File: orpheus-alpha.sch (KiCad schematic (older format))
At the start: 56 parts, among them J1 Signal in, J2 AC in, J3 Signal out, J4 uC, U1 OPA2134, U2 PGA2311, U3 LM317_3PinPackage, U4 LM337_SOT223, U5 LM7805_TO220

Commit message: Small changes, changed output coupling caps to film type
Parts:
- C12, C13: footprint Capacitors_THT:C_Disc_D7.5mm_W4.4mm_P5.00mm -> Capacitors_THT:C_Rect_L7.2mm_W7.2mm_P5.00mm_FKS2_FKP2_MKS2_MKP2
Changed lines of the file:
@@
 F 0 "C12" V 5950 1600 50  0000 C CNN
 F 1 "2.2u" V 5650 1550 50  0000 C CNN
-F 2 "Capacitors_THT:C_Disc_D7.5mm_W4.4mm_P5.00mm" H 5838 1450 50  0001 C CNN
+F 2 "Capacitors_THT:C_Rect_L7.2mm_W7.2mm_P5.00mm_FKS2_FKP2_MKS2_MKP2" H 5838 1450 50  0001 C CNN
 F 3 "" H 5800 1600 50  0001 C CNN
 	1    5800 1600
@@
 F 0 "C13" V 5950 2100 50  0000 C CNN
 F 1 "2.2u" V 5650 2050 50  0000 C CNN
-F 2 "Capacitors_THT:C_Disc_D7.5mm_W4.4mm_P5.00mm" H 5838 1950 50  0001 C CNN
+F 2 "Capacitors_THT:C_Rect_L7.2mm_W7.2mm_P5.00mm_FKS2_FKP2_MKS2_MKP2" H 5838 1950 50  0001 C CNN
 F 3 "" H 5800 2100 50  0001 C CNN
 	1    5800 2100

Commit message: Added part numbers
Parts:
- C1, C2, C3: footprint Capacitors_THT:CP_Radial_D5.0mm_P2.50mm -> Capacitors_THT:CP_Radial_D5.0mm_P2.00mm; Voltage (none) -> 10V; manf# (none) -> UPW1A101MDD
- C10, C11: manf# (none) -> CL10A106MO8NQNC
- C12, C13: manf# (none) -> MKS2C042201K00KSSD
- C14: Voltage (none) -> 25V; manf# (none) -> UBT1E471MPD8
- C15, C16, C8, C9: manf# (none) -> CL10B104JB8NNNC
- C4, C5, C6, C7: Voltage (none) -> 25V; manf# (none) -> UPW1E102MPD6
- Cd1, Cd2, Cd3, Cd4, Cd5: manf# (none) -> 06035C103JAT2A
- D1, D2, D3, D4, D5, D6, D7, D8: manf# (none) -> LL4004G
- D9: Current (none) -> 20mA; manf# (none) -> HSMA-C190
- J1, J3: manf# (none) -> 1715035
- J2: manf# (none) -> 1715022
- J4: manf# (none) -> M20-9970445
- R1, R2, R3, R4: Power (none) -> 1/4 W; Tolerance (none) -> 1%; manf# (none) -> CRCW06031K00FKEAHP
- R10, R7: Power (none) -> 1/4 W; Tolerance (none) -> 1%; manf# (none) -> ERJ-PA3F9100V
- R11: Power (none) -> 1/4 W; Tolerance (none) -> 1%; manf# (none) -> CRCW0603100RFKEAHP
- R12, R13: Power (none) -> 1/4 W; Tolerance (none) -> 1%; manf# (none) -> RCS0603300RFKEA
- R14, R15: Power (none) -> 1/4 W; Tolerance (none) -> 1%; manf# (none) -> CRCW0603100KFKEAHP
- R16: renamed from Rin1; Power (none) -> 1/4 W; Tolerance (none) -> 1%; manf# (none) -> CRCW060356K0FKEAHP
- R17: renamed from Rin2; Power (none) -> 1/4 W; Tolerance (none) -> 1%; manf# (none) -> CRCW060356K0FKEAHP
- R5, R6: Power (none) -> 1 W; Tolerance (none) -> 1%; manf# (none) -> WK73S2JTTE4R70F
- R8, R9: Power (none) -> 1/4 W; Tolerance (none) -> 1%; manf# (none) -> ESR03EZPF2701
- U1: manf# (none) -> OPA2134UA/2K5
- U2: manf# (none) -> PGA2311U
- U3: manf# (none) -> LM317DCYR
- U4: manf# (none) -> LM337IMP/NOPB
- U5: manf# (none) -> LM7805CT

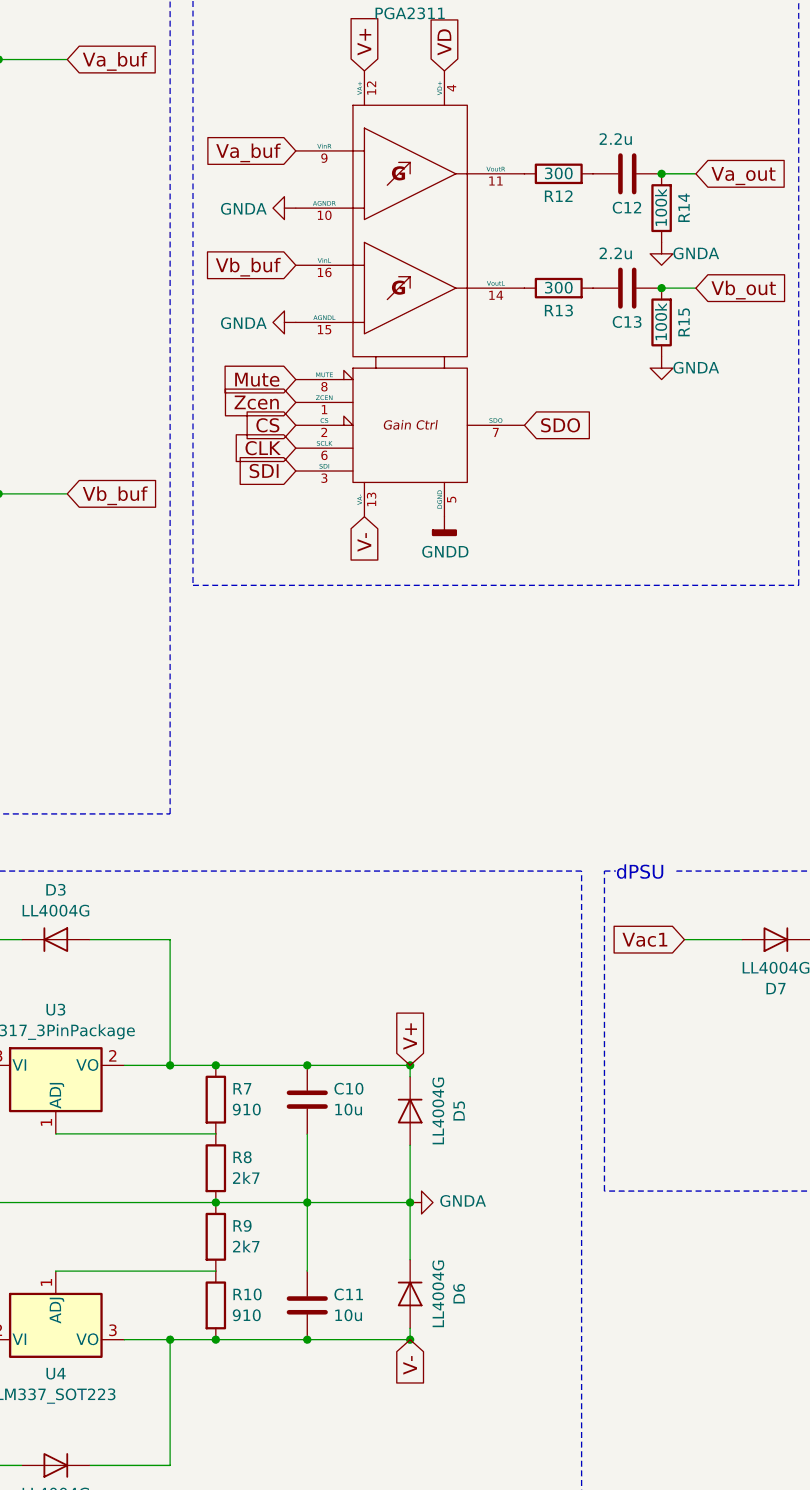
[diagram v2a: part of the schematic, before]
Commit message: Changed some part values and part numbers
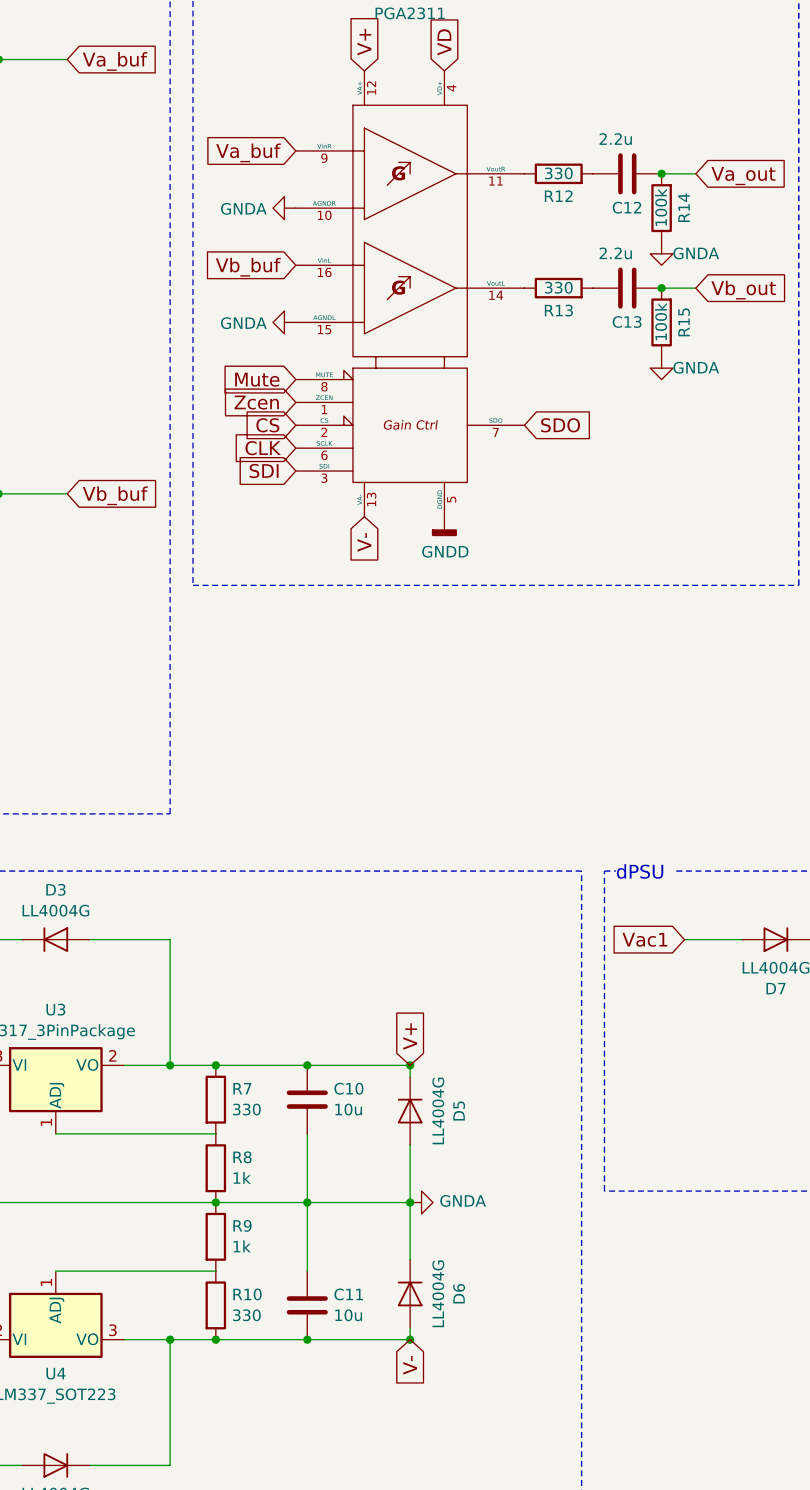
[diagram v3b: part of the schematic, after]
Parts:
- C1: Voltage 10V -> 16V; manf# UPW1A101MDD -> UFW1C101MDD1TD
- C14: manf# UBT1E471MPD8 -> UFW1E471MPD1TD
- C2, C3: Voltage 10V -> 16V; manf# UPW1A101MDD -> (none)
- C4: manf# UPW1E102MPD6 -> UFW1E102MPD
- C5, C6, C7: manf# UPW1E102MPD6 -> (none)
- D1: manf# LL4004G -> LL4004G L0
- D2, D3, D4, D5, D6, D7, D8: manf# LL4004G -> (none)
- R1: manf# CRCW06031K00FKEAHP -> RCA06031K00FKEAHP
- R10: value 910 -> 330; manf# ERJ-PA3F9100V -> (none)
- R11: manf# CRCW0603100RFKEAHP -> RCS0603100RFKEA
- R12, R13: value 300 -> 330; manf# RCS0603300RFKEA -> (none)
- R14: manf# CRCW0603100KFKEAHP -> ESR03EZPF1003
- R15: manf# CRCW0603100KFKEAHP -> (none)
- R16: manf# CRCW060356K0FKEAHP -> ERJ-PA3F5602V
- R17: manf# CRCW060356K0FKEAHP -> (none)
- R2, R3, R4: manf# CRCW06031K00FKEAHP -> (none)
- R5: manf# WK73S2JTTE4R70F -> RCL12184R70JNEK
- R6: manf# WK73S2JTTE4R70F -> (none)
- R7: value 910 -> 330; manf# ERJ-PA3F9100V -> ERJ-PA3F3300V
- R8, R9: value 2k7 -> 1k; manf# ESR03EZPF2701 -> (none)
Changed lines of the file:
@@
 F 4 "1%" H 1100 1400 60  0001 C CNN "Tolerance"
 F 5 "1/4 W" H 1100 1400 60  0001 C CNN "Power"
-F 6 "CRCW060356K0FKEAHP" H 1100 1400 60  0001 C CNN "manf#"
+F 6 "ERJ-PA3F5602V" H 1100 1400 60  0001 C CNN "manf#"
 	1    1100 1400
 	1    0    0    -1
@@
 F 4 "1%" H 1100 1400 60  0001 C CNN "Tolerance"
 F 5 "1/4 W" H 1100 1400 60  0001 C CNN "Power"
-F 6 "CRCW06031K00FKEAHP" H 1500 2000 60  0001 C CNN "manf#"
+F 6 "RCA06031K00FKEAHP" H 1500 2000 60  0001 C CNN "manf#"
 	1    1500 2000
 	-1   0    0    1
@@
 F 4 "1%" H 1100 1400 60  0001 C CNN "Tolerance"
 F 5 "1/4 W" H 1100 1400 60  0001 C CNN "Power"
-F 6 "CRCW06031K00FKEAHP" V 2150 1850 60  0001 C CNN "manf#"
 	1    2150 1850
 	0    -1   -1   0
@@
 F 2 "Capacitors_THT:CP_Radial_D5.0mm_P2.00mm" H 7338 1850 50  0001 C CNN
 F 3 "" H 7300 2000 50  0001 C CNN
-F 4 "UPW1A101MDD" H 7300 2000 60  0001 C CNN "manf#"
-F 5 "10V" H 7300 2000 60  0001 C CNN "Voltage"
+F 4 "UFW1C101MDD1TD" H 7300 2000 60  0001 C CNN "manf#"
+F 5 "16V" H 7300 2000 60  0001 C CNN "Voltage"
 	1    7300 2000
 	1    0    0    -1
@@
 F 2 "Capacitors_THT:CP_Radial_D5.0mm_P2.00mm" H 7338 2250 50  0001 C CNN
 F 3 "" H 7300 2400 50  0001 C CNN
-F 4 "UPW1A101MDD" H 7300 2400 60  0001 C CNN "manf#"
-F 5 "10V" H 7300 2400 60  0001 C CNN "Voltage"
+F 4 "16V" H 7300 2400 60  0001 C CNN "Voltage"
 	1    7300 2400
 	1    0    0    -1
@@
 F 4 "1%" H 1100 1400 60  0001 C CNN "Tolerance"
 F 5 "1/4 W" H 1100 1400 60  0001 C CNN "Power"
-F 6 "CRCW060356K0FKEAHP" H 1100 3300 60  0001 C CNN "manf#"
 	1    1100 3300
 	1    0    0    -1
@@
 F 4 "1%" H 1100 1400 60  0001 C CNN "Tolerance"
 F 5 "1/4 W" H 1100 1400 60  0001 C CNN "Power"
-F 6 "CRCW06031K00FKEAHP" H 1500 3900 60  0001 C CNN "manf#"
 	1    1500 3900
 	-1   0    0    1
@@
 F 4 "1%" H 1100 1400 60  0001 C CNN "Tolerance"
 F 5 "1/4 W" H 1100 1400 60  0001 C CNN "Power"
-F 6 "CRCW06031K00FKEAHP" V 2150 3750 60  0001 C CNN "manf#"
 	1    2150 3750
 	0    -1   -1   0
@@
 F 2 "Capacitors_THT:CP_Radial_D5.0mm_P2.00mm" H 8938 2000 50  0001 C CNN
 F 3 "" H 8900 2150 50  0001 C CNN
-F 4 "UPW1A101MDD" H 8900 2150 60  0001 C CNN "manf#"
-F 5 "10V" H 8900 2150 60  0001 C CNN "Voltage"
+F 4 "16V" H 8900 2150 60  0001 C CNN "Voltage"
 	1    8900 2150
 	1    0    0    -1
@@
 F 2 "Diodes_SMD:D_MELF_Handsoldering" H 900 5700 50  0001 C CNN
 F 3 "http://www.mouser.com/ds/2/395/LL4001G%20SERIES_E15-1112814.pdf" H 900 5700 50  0001 C CNN
-F 4 "LL4004G" H 900 5700 60  0001 C CNN "manf#"
+F 4 "LL4004G L0" H 900 5700 60  0001 C CNN "manf#"
 	1    900  5700
 	0    1    1    0
@@
 F 2 "Diodes_SMD:D_MELF_Handsoldering" H 900 6500 50  0001 C CNN
 F 3 "http://www.mouser.com/ds/2/395/LL4001G%20SERIES_E15-1112814.pdf" H 900 5700 50  0001 C CNN
-F 4 "LL4004G" H 900 5700 60  0001 C CNN "manf#"
 	1    900  6500
 	0    1    1    0
@@
 F 2 "Diodes_SMD:D_MELF_Handsoldering" H 4850 5700 50  0001 C CNN
 F 3 "http://www.mouser.com/ds/2/395/LL4001G%20SERIES_E15-1112814.pdf" H 900 5700 50  0001 C CNN
-F 4 "LL4004G" H 900 5700 60  0001 C CNN "manf#"
 	1    4850 5700
 	0    1    1    0
@@
 F 2 "Diodes_SMD:D_MELF_Handsoldering" H 4850 6500 50  0001 C CNN
 F 3 "http://www.mouser.com/ds/2/395/LL4001G%20SERIES_E15-1112814.pdf" H 900 5700 50  0001 C CNN
-F 4 "LL4004G" H 900 5700 60  0001 C CNN "manf#"
 	1    4850 6500
 	0    1    1    0
@@
 F 2 "Diodes_SMD:D_MELF_Handsoldering" H 3300 4950 50  0001 C CNN
 F 3 "http://www.mouser.com/ds/2/395/LL4001G%20SERIES_E15-1112814.pdf" H 900 5700 50  0001 C CNN
-F 4 "LL4004G" H 900 5700 60  0001 C CNN "manf#"
 	1    3300 4950
 	1    0    0    -1
@@
 F 2 "Diodes_SMD:D_MELF_Handsoldering" H 3300 7250 50  0001 C CNN
 F 3 "http://www.mouser.com/ds/2/395/LL4001G%20SERIES_E15-1112814.pdf" H 900 5700 50  0001 C CNN
-F 4 "LL4004G" H 900 5700 60  0001 C CNN "manf#"
 	1    3300 7250
 	-1   0    0    1
@@
 F 4 "1%" H 1100 1400 60  0001 C CNN "Tolerance"
 F 5 "1 W" H 1100 1400 60  0001 C CNN "Power"
-F 6 "WK73S2JTTE4R70F" V 1700 5500 60  0001 C CNN "manf#"
+F 6 "RCL12184R70JNEK" V 1700 5500 60  0001 C CNN "manf#"
 	1    1700 5500
 	0    -1   -1   0
@@
 F 4 "1%" H 1100 1400 60  0001 C CNN "Tolerance"
 F 5 "1 W" H 1100 1400 60  0001 C CNN "Power"
-F 6 "WK73S2JTTE4R70F" V 1700 6700 60  0001 C CNN "manf#"
 	1    1700 6700
 	0    -1   -1   0
@@
 P 4000 5650
 F 0 "R7" H 4070 5696 50  0000 L CNN
-F 1 "910" H 4070 5605 50  0000 L CNN
+F 1 "330" H 4070 5605 50  0000 L CNN
 F 2 "Resistors_SMD:R_0603_HandSoldering" V 3930 5650 50  0001 C CNN
 F 3 "" H 4000 5650 50  0001 C CNN
 F 4 "1%" H 1100 1400 60  0001 C CNN "Tolerance"
 F 5 "1/4 W" H 1100 1400 60  0001 C CNN "Power"
-F 6 "ERJ-PA3F9100V" H 4000 5650 60  0001 C CNN "manf#"
+F 6 "ERJ-PA3F3300V" H 4000 5650 60  0001 C CNN "manf#"
 	1    4000 5650
 	1    0    0    -1
@@
 P 4000 6550
 F 0 "R10" H 4070 6596 50  0000 L CNN
-F 1 "910" H 4070 6505 50  0000 L CNN
+F 1 "330" H 4070 6505 50  0000 L CNN
 F 2 "Resistors_SMD:R_0603_HandSoldering" V 3930 6550 50  0001 C CNN
 F 3 "" H 4000 6550 50  0001 C CNN
 F 4 "1%" H 1100 1400 60  0001 C CNN "Tolerance"
 F 5 "1/4 W" H 1100 1400 60  0001 C CNN "Power"
-F 6 "ERJ-PA3F9100V" H 4000 6550 60  0001 C CNN "manf#"
 	1    4000 6550
 	1    0    0    -1
@@
 P 4000 6250
 F 0 "R9" H 4070 6296 50  0000 L CNN
-F 1 "2k7" H 4070 6205 50  0000 L CNN
+F 1 "1k" H 4070 6205 50  0000 L CNN
 F 2 "Resistors_SMD:R_0603_HandSoldering" V 3930 6250 50  0001 C CNN
 F 3 "" H 4000 6250 50  0001 C CNN
 F 4 "1%" H 1100 1400 60  0001 C CNN "Tolerance"
 F 5 "1/4 W" H 1100 1400 60  0001 C CNN "Power"
-F 6 "ESR03EZPF2701" H 4000 6250 60  0001 C CNN "manf#"
 	1    4000 6250
 	1    0    0    -1
@@
 P 4000 5950
 F 0 "R8" H 4070 5996 50  0000 L CNN
-F 1 "2k7" H 4070 5905 50  0000 L CNN
+F 1 "1k" H 4070 5905 50  0000 L CNN
 F 2 "Resistors_SMD:R_0603_HandSoldering" V 3930 5950 50  0001 C CNN
 F 3 "" H 4000 5950 50  0001 C CNN
 F 4 "1%" H 1100 1400 60  0001 C CNN "Tolerance"
 F 5 "1/4 W" H 1100 1400 60  0001 C CNN "Power"
-F 6 "ESR03EZPF2701" H 4000 5950 60  0001 C CNN "manf#"
 	1    4000 5950
 	1    0    0    -1
@@
 F 3 "" H 2100 5650 50  0001 C CNN
 F 4 "25V" H 1350 5650 60  0001 C CNN "Voltage"
-F 5 "UPW1E102MPD6" H 1350 5650 60  0001 C CNN "manf#"
 	1    2100 5650
 	1    0    0    -1
@@
 F 3 "" H 2100 6550 50  0001 C CNN
 F 4 "25V" H 1350 5650 60  0001 C CNN "Voltage"
-F 5 "UPW1E102MPD6" H 1350 5650 60  0001 C CNN "manf#"
 	1    2100 6550
 	1    0    0    -1
@@
 F 3 "" H 1350 5650 50  0001 C CNN
 F 4 "25V" H 1350 5650 60  0001 C CNN "Voltage"
-F 5 "UPW1E102MPD6" H 1350 5650 60  0001 C CNN "manf#"
+F 5 "UFW1E102MPD" H 1350 5650 60  0001 C CNN "manf#"
 	1    1350 5650
 	1    0    0    -1
@@
 F 3 "" H 1350 6550 50  0001 C CNN
 F 4 "25V" H 1350 5650 60  0001 C CNN "Voltage"
-F 5 "UPW1E102MPD6" H 1350 5650 60  0001 C CNN "manf#"
 	1    1350 6550
 	1    0    0    -1
@@
 F 2 "Diodes_SMD:D_MELF_Handsoldering" H 6450 4950 50  0001 C CNN
 F 3 "http://www.mouser.com/ds/2/395/LL4001G%20SERIES_E15-1112814.pdf" H 900 5700 50  0001 C CNN
-F 4 "LL4004G" H 900 5700 60  0001 C CNN "manf#"
 	1    6450 4950
 	-1   0    0    1
@@
 F 2 "Capacitors_THT:CP_Radial_D10.0mm_P7.50mm" H 6988 4950 50  0001 C CNN
 F 3 "" H 6950 5100 50  0001 C CNN
-F 4 "UBT1E471MPD8" H 6950 5100 60  0001 C CNN "manf#"
+F 4 "UFW1E471MPD1TD" H 6950 5100 60  0001 C CNN "manf#"
 F 5 "25V" H 6950 5100 60  0001 C CNN "Voltage"
 	1    6950 5100
@@
 F 2 "Diodes_SMD:D_MELF_Handsoldering" H 8050 5550 50  0001 C CNN
 F 3 "http://www.mouser.com/ds/2/395/LL4001G%20SERIES_E15-1112814.pdf" H 900 5700 50  0001 C CNN
-F 4 "LL4004G" H 900 5700 60  0001 C CNN "manf#"
 	1    8050 5550
 	1    0    0    -1
@@
 F 4 "1%" H 1100 1400 60  0001 C CNN "Tolerance"
 F 5 "1/4 W" H 1100 1400 60  0001 C CNN "Power"
-F 6 "CRCW0603100RFKEAHP" V 9250 5100 60  0001 C CNN "manf#"
+F 6 "RCS0603100RFKEA" V 9250 5100 60  0001 C CNN "manf#"
 	1    9250 5100
 	1    0    0    -1
@@
 P 5500 1600
 F 0 "R12" V 5400 1600 50  0000 C CNN
-F 1 "300" V 5500 1600 50  0000 C CNN
+F 1 "330" V 5500 1600 50  0000 C CNN
 F 2 "Resistors_SMD:R_0603_HandSoldering" V 5430 1600 50  0001 C CNN
 F 3 "" H 5500 1600 50  0001 C CNN
 F 4 "1%" H 1100 1400 60  0001 C CNN "Tolerance"
 F 5 "1/4 W" H 1100 1400 60  0001 C CNN "Power"
-F 6 "RCS0603300RFKEA" V 5500 1600 60  0001 C CNN "manf#"
 	1    5500 1600
 	0    -1   -1   0
@@
 P 5500 2100
 F 0 "R13" V 5400 2100 50  0000 C CNN
-F 1 "300" V 5500 2100 50  0000 C CNN
+F 1 "330" V 5500 2100 50  0000 C CNN
 F 2 "Resistors_SMD:R_0603_HandSoldering" V 5430 2100 50  0001 C CNN
 F 3 "" H 5500 2100 50  0001 C CNN
 F 4 "1%" H 1100 1400 60  0001 C CNN "Tolerance"
 F 5 "1/4 W" H 1100 1400 60  0001 C CNN "Power"
-F 6 "RCS0603300RFKEA" V 5500 2100 60  0001 C CNN "manf#"
 	1    5500 2100
 	0    -1   -1   0
@@
 F 4 "1%" H 1100 1400 60  0001 C CNN "Tolerance"
 F 5 "1/4 W" H 1100 1400 60  0001 C CNN "Power"
-F 6 "CRCW0603100KFKEAHP" V 5950 1750 60  0001 C CNN "manf#"
+F 6 "ESR03EZPF1003" V 5950 1750 60  0001 C CNN "manf#"
 	1    5950 1750
 	-1   0    0    1
@@
 F 4 "1%" H 1100 1400 60  0001 C CNN "Tolerance"
 F 5 "1/4 W" H 1100 1400 60  0001 C CNN "Power"
-F 6 "CRCW0603100KFKEAHP" V 5950 2250 60  0001 C CNN "manf#"
 	1    5950 2250
 	-1   0    0    1
